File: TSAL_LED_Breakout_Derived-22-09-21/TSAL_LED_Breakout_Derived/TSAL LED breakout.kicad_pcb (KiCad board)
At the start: 2 copper layers, 33 x 25 mm, 22 parts, among them J1 Conn_01x03, U1 PAM2804, U2 PAM2804

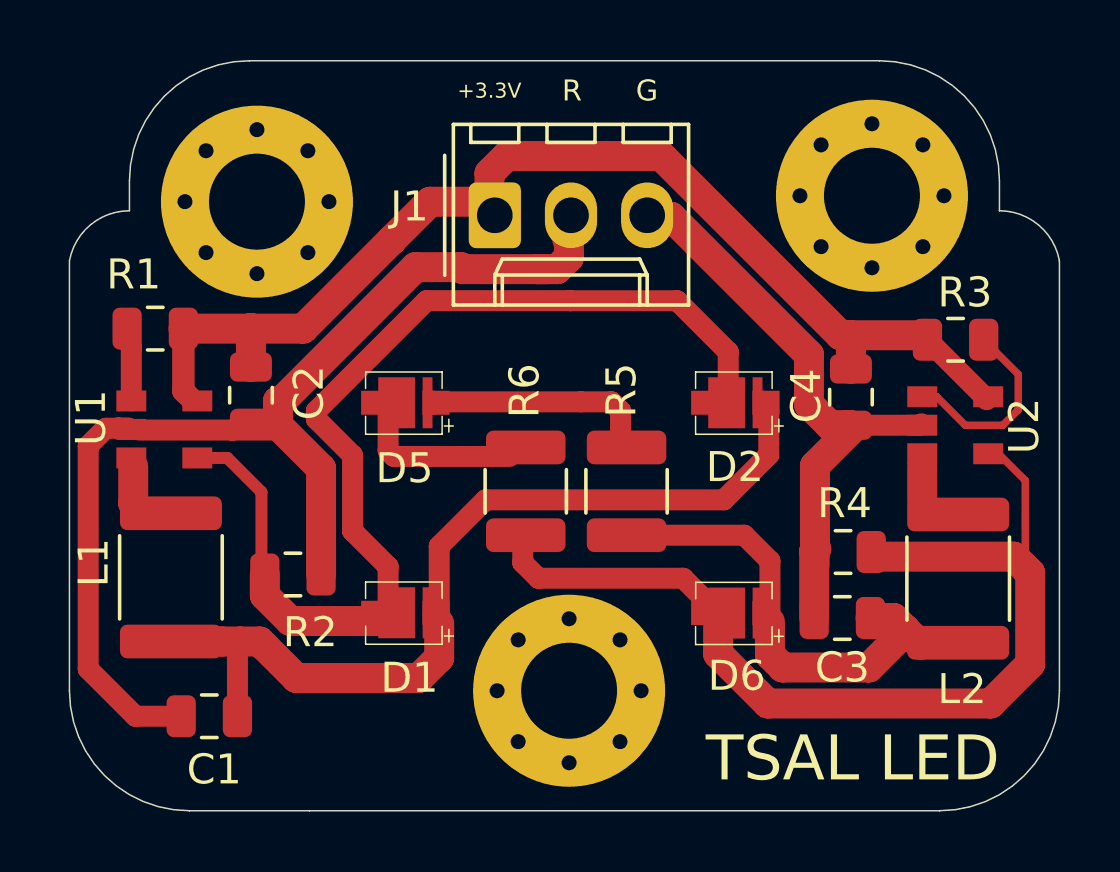
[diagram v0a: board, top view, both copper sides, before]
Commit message: fix: improved traces TSAL LED
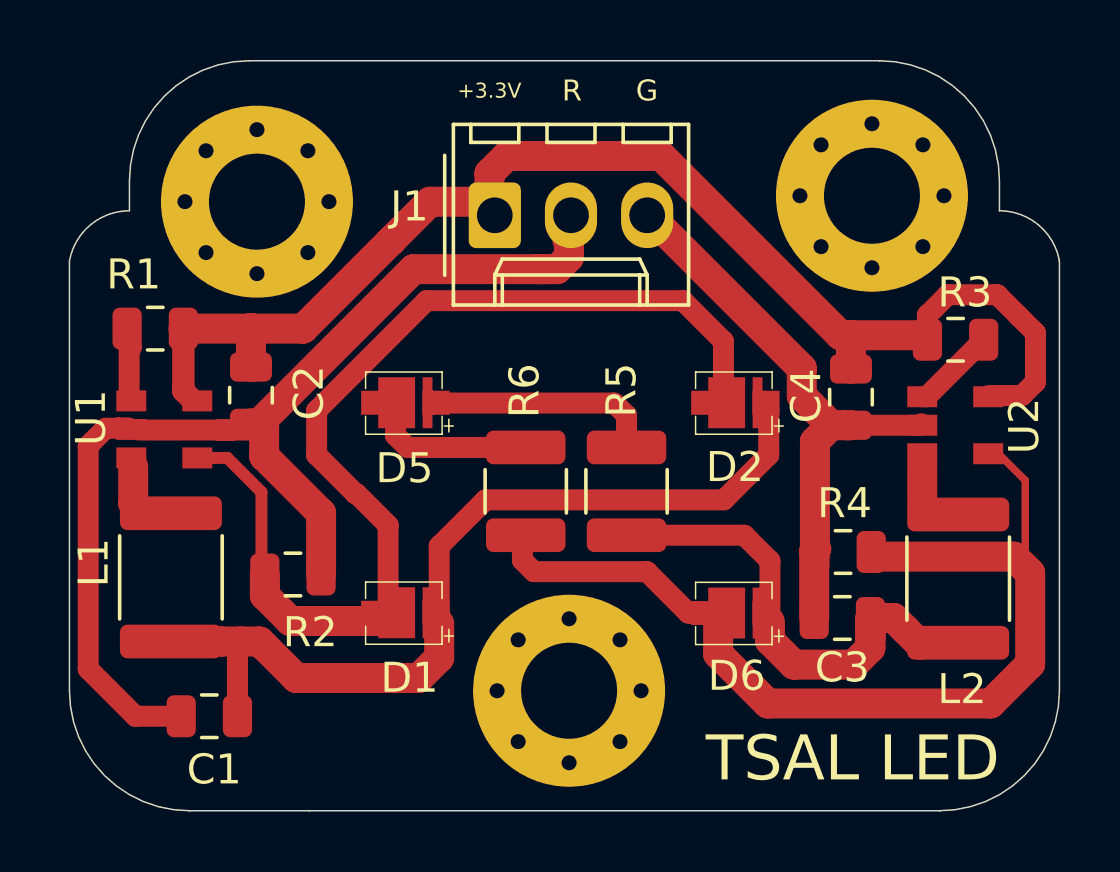
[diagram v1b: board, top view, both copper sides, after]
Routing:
- net +3V3: track 38.5 -> 44.3 mm
- net Net-(R3-Pad2): track 6.34 -> 2.69 mm
- net Path_Green: track 20.2 -> 19.4 mm
